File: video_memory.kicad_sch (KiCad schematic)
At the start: 23 parts

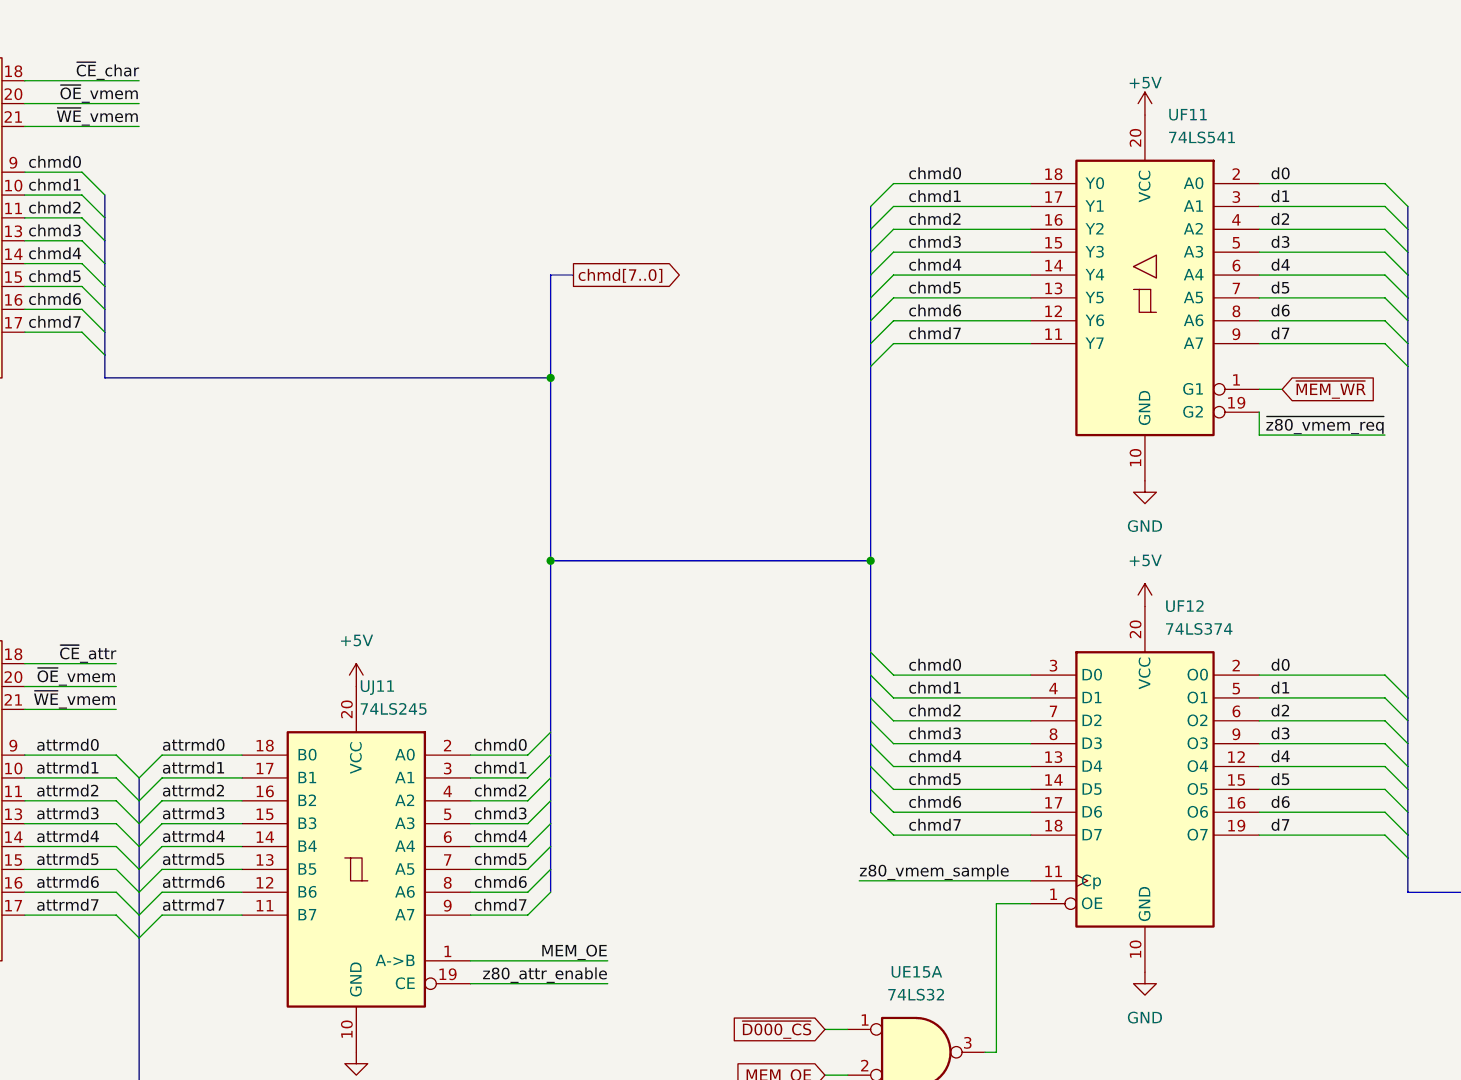
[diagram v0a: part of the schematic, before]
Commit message: Fixed some wrong labels
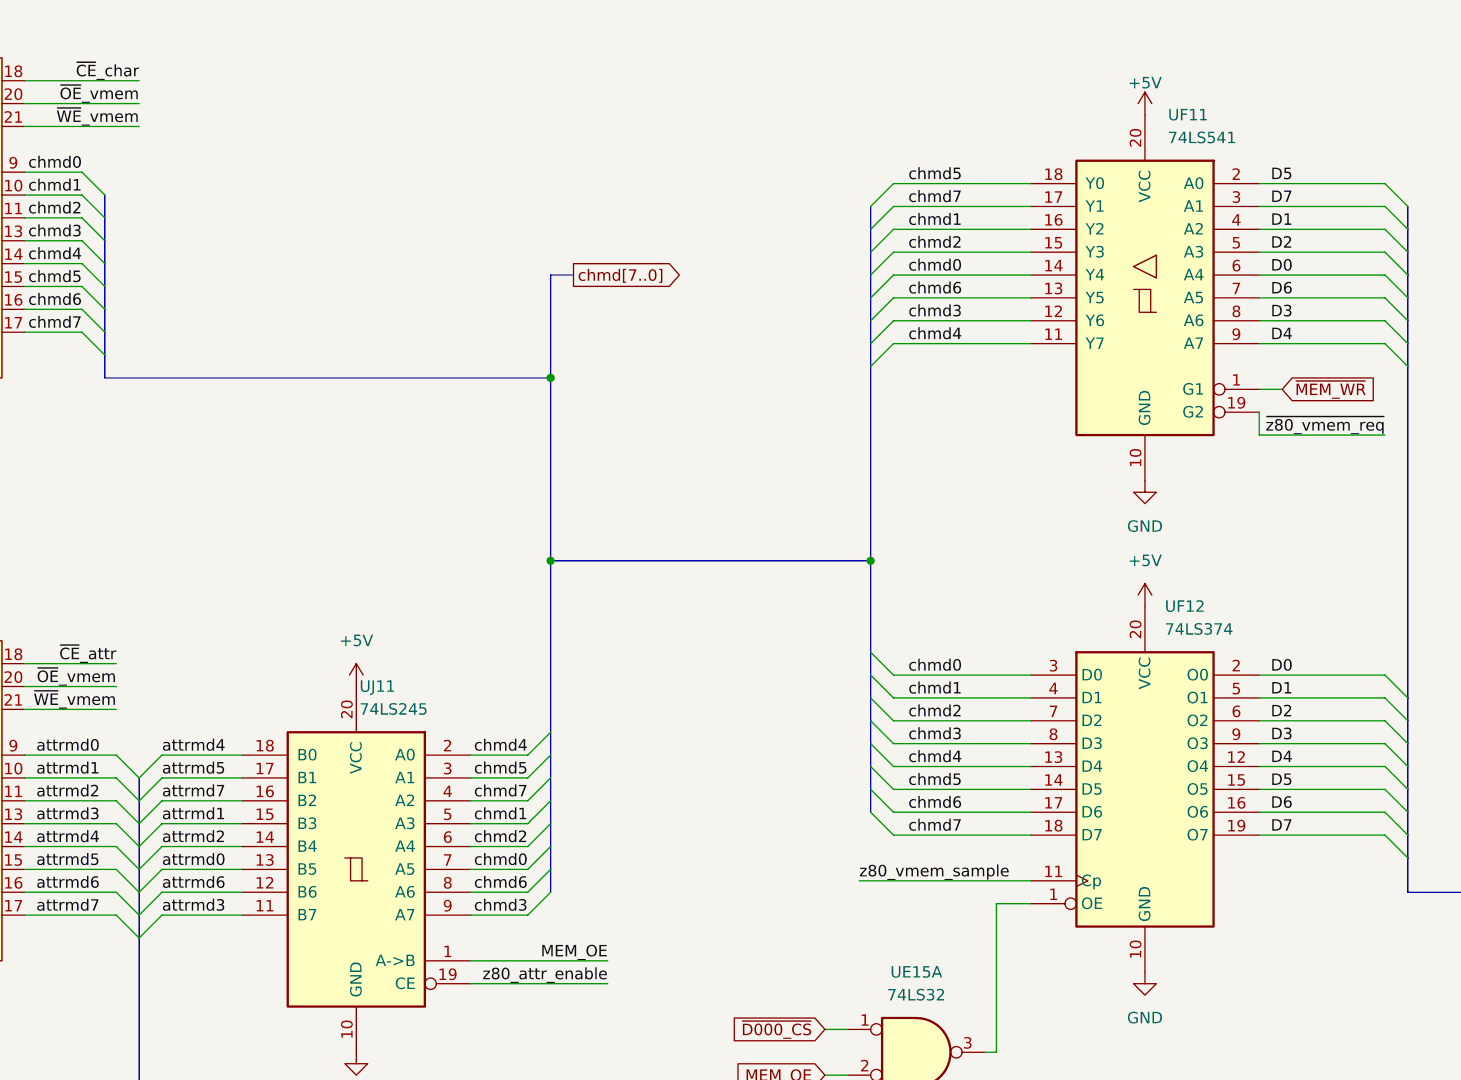
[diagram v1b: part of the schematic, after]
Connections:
- net attrmd0: now also UJ11.13 (B5); no longer UJ11.18 (B0)
- net attrmd1: now also UJ11.15 (B3); no longer UJ11.17 (B1)
- net attrmd2: now also UJ11.14 (B4); no longer UJ11.16 (B2)
- net attrmd3: now also UJ11.11 (B7); no longer UJ11.15 (B3)
- net attrmd4: now also UJ11.18 (B0); no longer UJ11.14 (B4)
- net attrmd5: now also UJ11.17 (B1); no longer UJ11.13 (B5)
- net attrmd7: now also UJ11.16 (B2); no longer UJ11.11 (B7)
- net chmd0: now also UF11.14 (Y4), UJ11.7 (A5); no longer UF11.18 (Y0), UJ11.2 (A0)
- net chmd1: now also UF11.16 (Y2), UJ11.5 (A3); no longer UF11.17 (Y1), UJ11.3 (A1)
- net chmd2: now also UF11.15 (Y3), UJ11.6 (A4); no longer UF11.16 (Y2), UJ11.4 (A2)
- net chmd3: now also UF11.12 (Y6), UJ11.9 (A7); no longer UF11.15 (Y3), UJ11.5 (A3)
- net chmd4: now also UF11.11 (Y7), UJ11.2 (A0); no longer UF11.14 (Y4), UJ11.6 (A4)
- net chmd5: now also UF11.18 (Y0), UJ11.3 (A1); no longer UF11.13 (Y5), UJ11.7 (A5)
- net chmd6: now also UF11.13 (Y5); no longer UF11.12 (Y6)
- net chmd7: now also UF11.17 (Y1), UJ11.4 (A2); no longer UF11.11 (Y7), UJ11.9 (A7)
- net d0 renamed D0
- net D0: now also UF11.6 (A4); no longer UF11.2 (A0)
- net d1 renamed D1
- net D1: now also UF11.4 (A2); no longer UF11.3 (A1)
- net d2 renamed D2
- net D2: now also UF11.5 (A3); no longer UF11.4 (A2)
- net d3 renamed D3
- net D3: now also UF11.8 (A6); no longer UF11.5 (A3)
- net d4 renamed D4
- net D4: now also UF11.9 (A7); no longer UF11.6 (A4)
- net d5 renamed D5
- net D5: now also UF11.2 (A0); no longer UF11.7 (A5)
- net d6 renamed D6
- net D6: now also UF11.7 (A5); no longer UF11.8 (A6)
- net d7 renamed D7
- net D7: now also UF11.3 (A1); no longer UF11.9 (A7)
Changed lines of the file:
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@@
 		)
 	)
-	(label "chmd4"
+	(label "chmd2"
 		(at 240.03 111.76 180)
 		(effects
@@
 		)
 	)
-	(label "attrmd0"
+	(label "attrmd4"
 		(at 199.39 101.6 0)
 		(effects
@@
 		)
 	)
-	(label "d6"
+	(label "D3"
 		(at 322.58 53.34 0)
 		(effects
@@
 		)
 	)
-	(label "chmd1"
+	(label "chmd5"
 		(at 240.03 104.14 180)
 		(effects
@@
 		)
 	)
-	(label "d4"
+	(label "D4"
 		(at 322.58 102.87 0)
 		(effects
@@
 		)
 	)
-	(label "d2"
+	(label "D2"
 		(at 322.58 97.79 0)
 		(effects
@@
 		)
 	)
-	(label "chmd1"
+	(label "chmd7"
 		(at 288.29 40.64 180)
 		(effects
@@
 		)
 	)
-	(label "chmd0"
+	(label "chmd5"
 		(at 288.29 38.1 180)
 		(effects
@@
 		)
 	)
-	(label "chmd5"
+	(label "chmd0"
 		(at 240.03 114.3 180)
 		(effects
@@
 		)
 	)
-	(label "d5"
+	(label "D6"
 		(at 322.58 50.8 0)
 		(effects
@@
 		)
 	)
-	(label "d7"
+	(label "D4"
 		(at 322.58 55.88 0)
 		(effects
@@
 		)
 	)
-	(label "chmd3"
+	(label "chmd1"
 		(at 240.03 109.22 180)
 		(effects
@@
 		)
 	)
-	(label "d0"
+	(label "D0"
 		(at 322.58 92.71 0)
 		(effects
@@
 		)
 	)
-	(label "chmd4"
+	(label "chmd0"
 		(at 288.29 48.26 180)
 		(effects
@@
 		)
 	)
-	(label "d1"
+	(label "D7"
 		(at 322.58 40.64 0)
 		(effects
@@
 		)
 	)
-	(label "d2"
+	(label "D1"
 		(at 322.58 43.18 0)
 		(effects
@@
 		)
 	)
-	(label "d3"
+	(label "D2"
 		(at 322.58 45.72 0)
 		(effects
@@
 		)
 	)
-	(label "chmd7"
+	(label "chmd4"
 		(at 288.29 55.88 180)
 		(effects
@@
 		)
 	)
-	(label "d6"
+	(label "D6"
 		(at 322.58 107.95 0)
 		(effects
@@
 		)
 	)
-	(label "chmd2"
+	(label "chmd7"
 		(at 240.03 106.68 180)
 		(effects
@@
 		)
 	)
-	(label "d7"
+	(label "D7"
 		(at 322.58 110.49 0)
 		(effects
@@
 		)
 	)
-	(label "d3"
+	(label "D3"
 		(at 322.58 100.33 0)
 		(effects
@@
 		)
 	)
-	(label "chmd5"
+	(label "chmd6"
 		(at 288.29 50.8 180)
 		(effects
@@
 		)
 	)
-	(label "attrmd5"
+	(label "attrmd0"
 		(at 199.39 114.3 0)
 		(effects
@@
 		)
 	)
-	(label "d5"
+	(label "D5"
 		(at 322.58 105.41 0)
 		(effects
@@
 		)
 	)
-	(label "chmd6"
+	(label "chmd3"
 		(at 288.29 53.34 180)
 		(effects
@@
 		)
 	)
-	(label "attrmd3"
+	(label "attrmd1"
 		(at 199.39 109.22 0)
 		(effects
@@
 		)
 	)
-	(label "chmd0"
+	(label "chmd4"
 		(at 240.03 101.6 180)
 		(effects
@@
 		)
 	)
-	(label "attrmd7"
+	(label "attrmd3"
 		(at 199.39 119.38 0)
 		(effects
@@
 		)
 	)
-	(label "attrmd1"
+	(label "attrmd5"
 		(at 199.39 104.14 0)
 		(effects
@@
 		)
 	)
-	(label "chmd3"
+	(label "chmd2"
 		(at 288.29 45.72 180)
 		(effects
@@
 		)
 	)
-	(label "d4"
+	(label "D0"
 		(at 322.58 48.26 0)
 		(effects
@@
 		)
 	)
-	(label "chmd7"
+	(label "chmd3"
 		(at 240.03 119.38 180)
 		(effects
@@
 		)
 	)
-	(label "attrmd2"
+	(label "attrmd7"
 		(at 199.39 106.68 0)
 		(effects
@@
 		)
 	)
-	(label "chmd2"
+	(label "chmd1"
 		(at 288.29 43.18 180)
 		(effects
@@
 		)
 	)
-	(label "attrmd4"
+	(label "attrmd2"
 		(at 199.39 111.76 0)
 		(effects
@@
 		)
 	)
-	(label "d1"
+	(label "D1"
 		(at 322.58 95.25 0)
 		(effects
@@
 		)
 	)
-	(label "d0"
+	(label "D5"
 		(at 322.58 38.1 0)
 		(effects

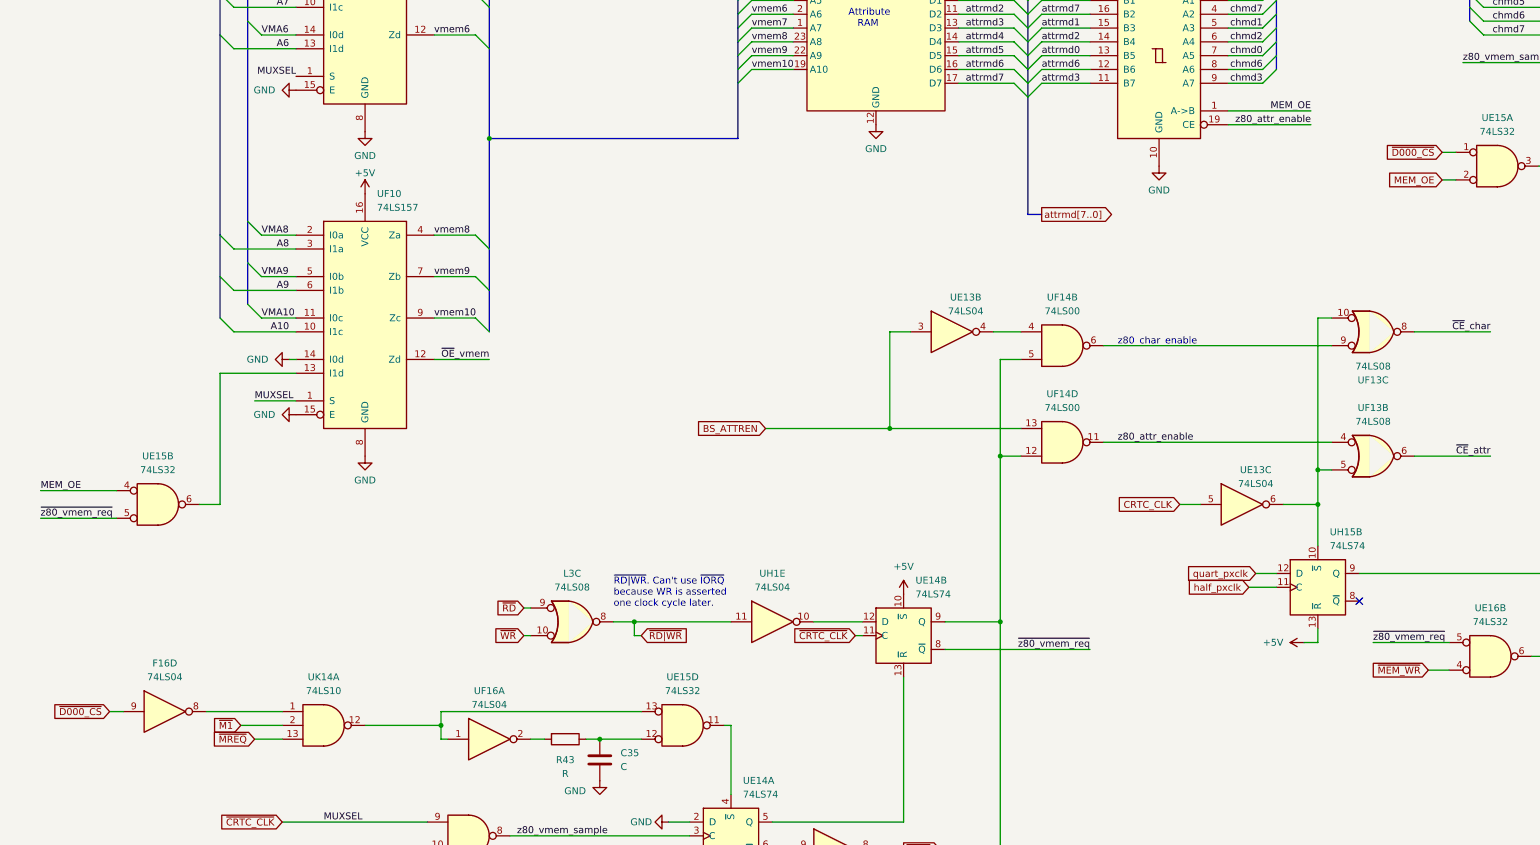
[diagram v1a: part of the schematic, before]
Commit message: Corrected MEM_OE and MREQ labels
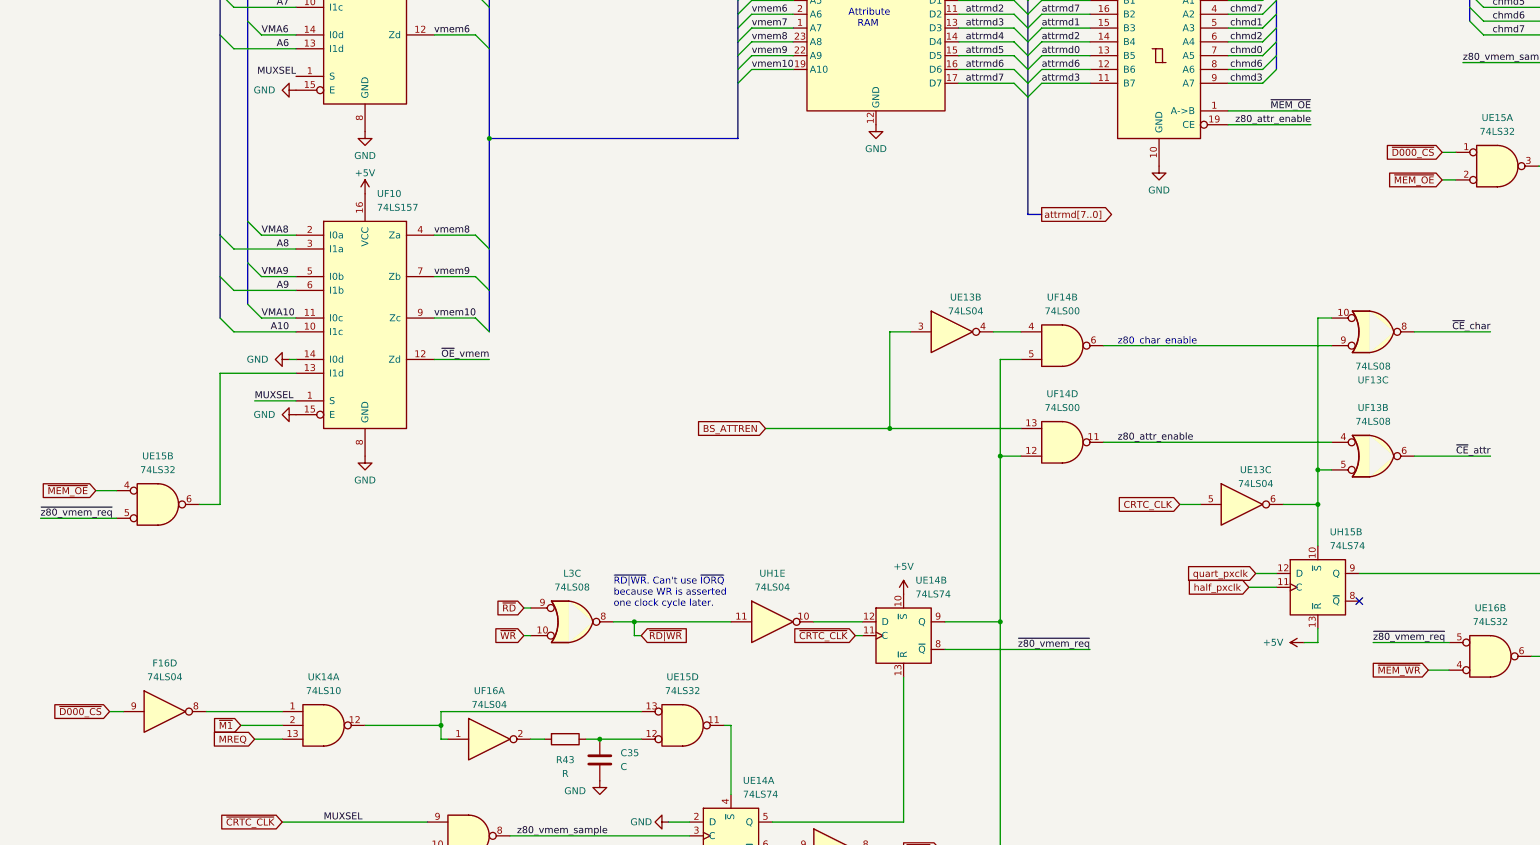
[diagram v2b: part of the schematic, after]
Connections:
- net MEM_OE renamed ~{MEM_OE}
- net ~{MREQ} renamed MREQ
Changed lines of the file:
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@@
 	(wire
 		(pts
-			(xy 15.24 194.31) (xy 29.21 194.31)
+			(xy 25.4 194.31) (xy 29.21 194.31)
 		)
 		(stroke
@@
 		)
 	)
-	(label "MEM_OE"
-		(at 15.24 194.31 0)
-		(effects
-			(font
-				(size 1.27 1.27)
-			)
-			(justify left bottom)
-		)
-	)
 	(label "VMA2"
 		(at 55.88 50.8 0)
@@
 		)
 	)
-	(label "MEM_OE"
+	(label "~{MEM_OE}"
 		(at 248.92 124.46 180)
 		(effects
@@
 		)
 	)
-	(global_label "~{MREQ}"
+	(global_label "MREQ"
 		(shape input)
 		(at 54.61 240.03 180)
@@
 		)
 	)
+	(global_label "~{MEM_OE}"
+		(shape input)
+		(at 25.4 194.31 180)
+		(fields_autoplaced yes)
+		(effects
+			(font
+				(size 1.27 1.27)
+			)
+			(justify right)
+		)
+		(property "Intersheetrefs" "${INTERSHEET_REFS}"
+			(at 14.9159 194.31 0)
+			(effects
+				(font
+					(size 1.27 1.27)
+				)
+				(justify right)
+				(hide yes)
+			)
+		)
+	)
 	(global_label "~{WR}"
 		(shape input)
@@
 		)
 	)
-	(global_label "MEM_OE"
+	(global_label "~{MEM_OE}"
 		(shape input)
 		(at 273.05 137.16 180)
